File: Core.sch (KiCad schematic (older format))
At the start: 2 parts

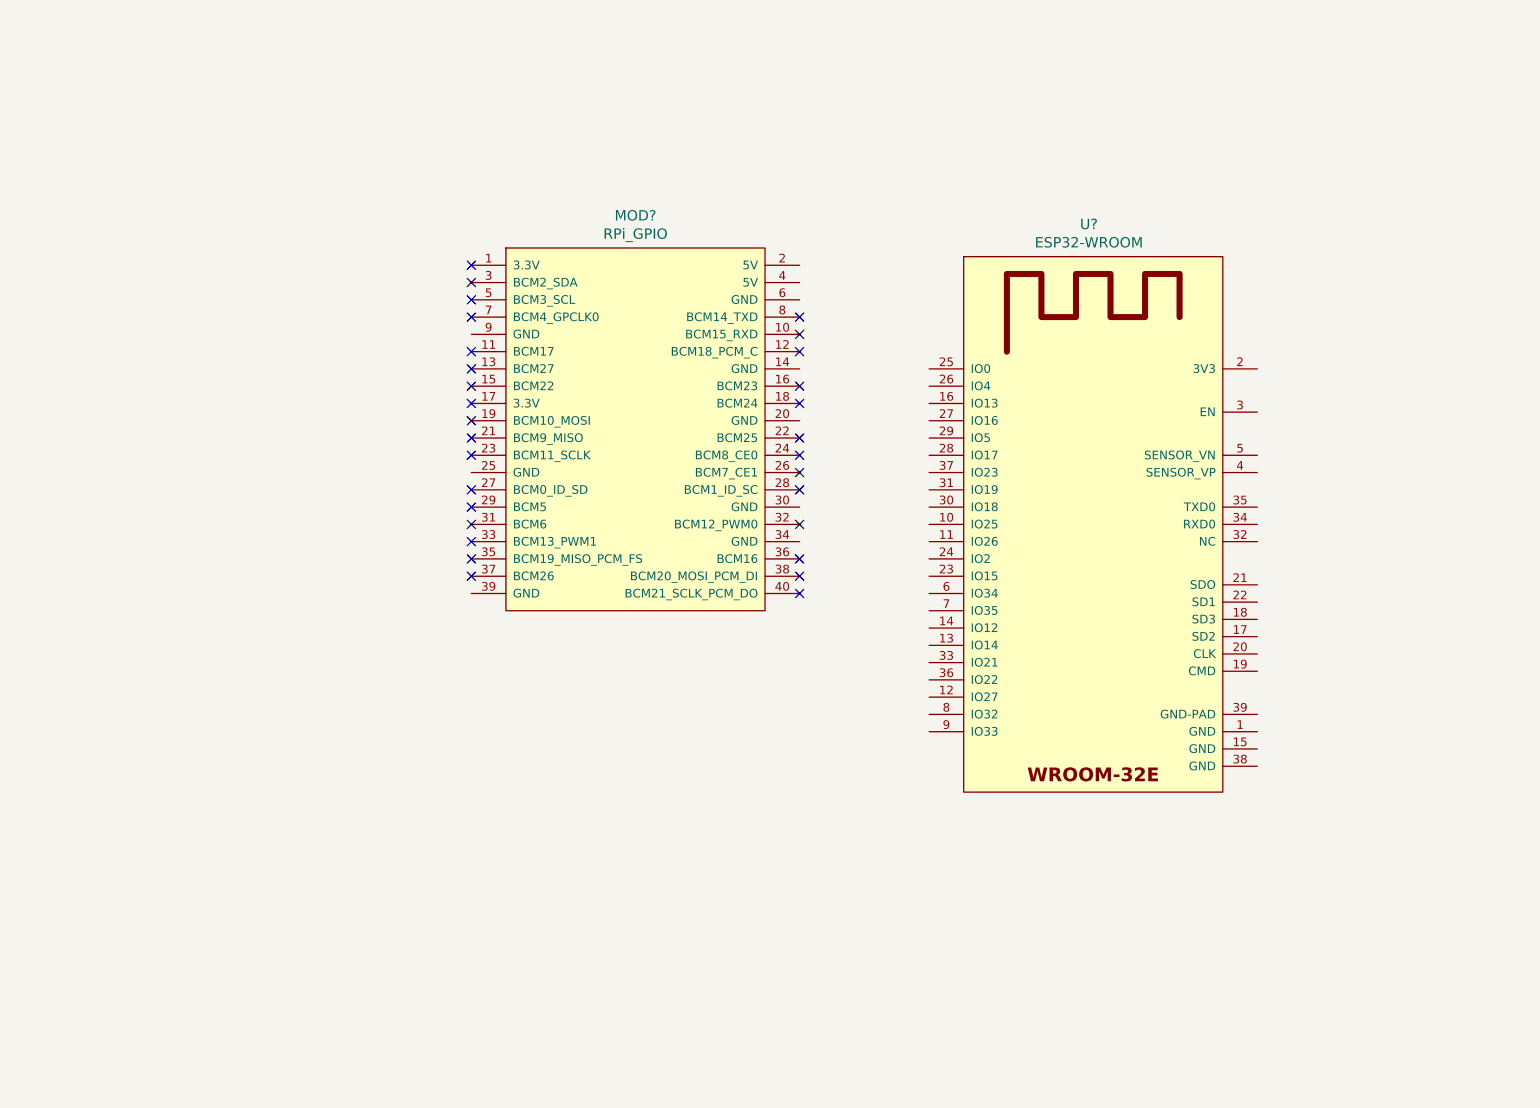
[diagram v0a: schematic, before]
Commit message: Arreglos.
    * Arreglo referencias de address de salida(PCF8574)
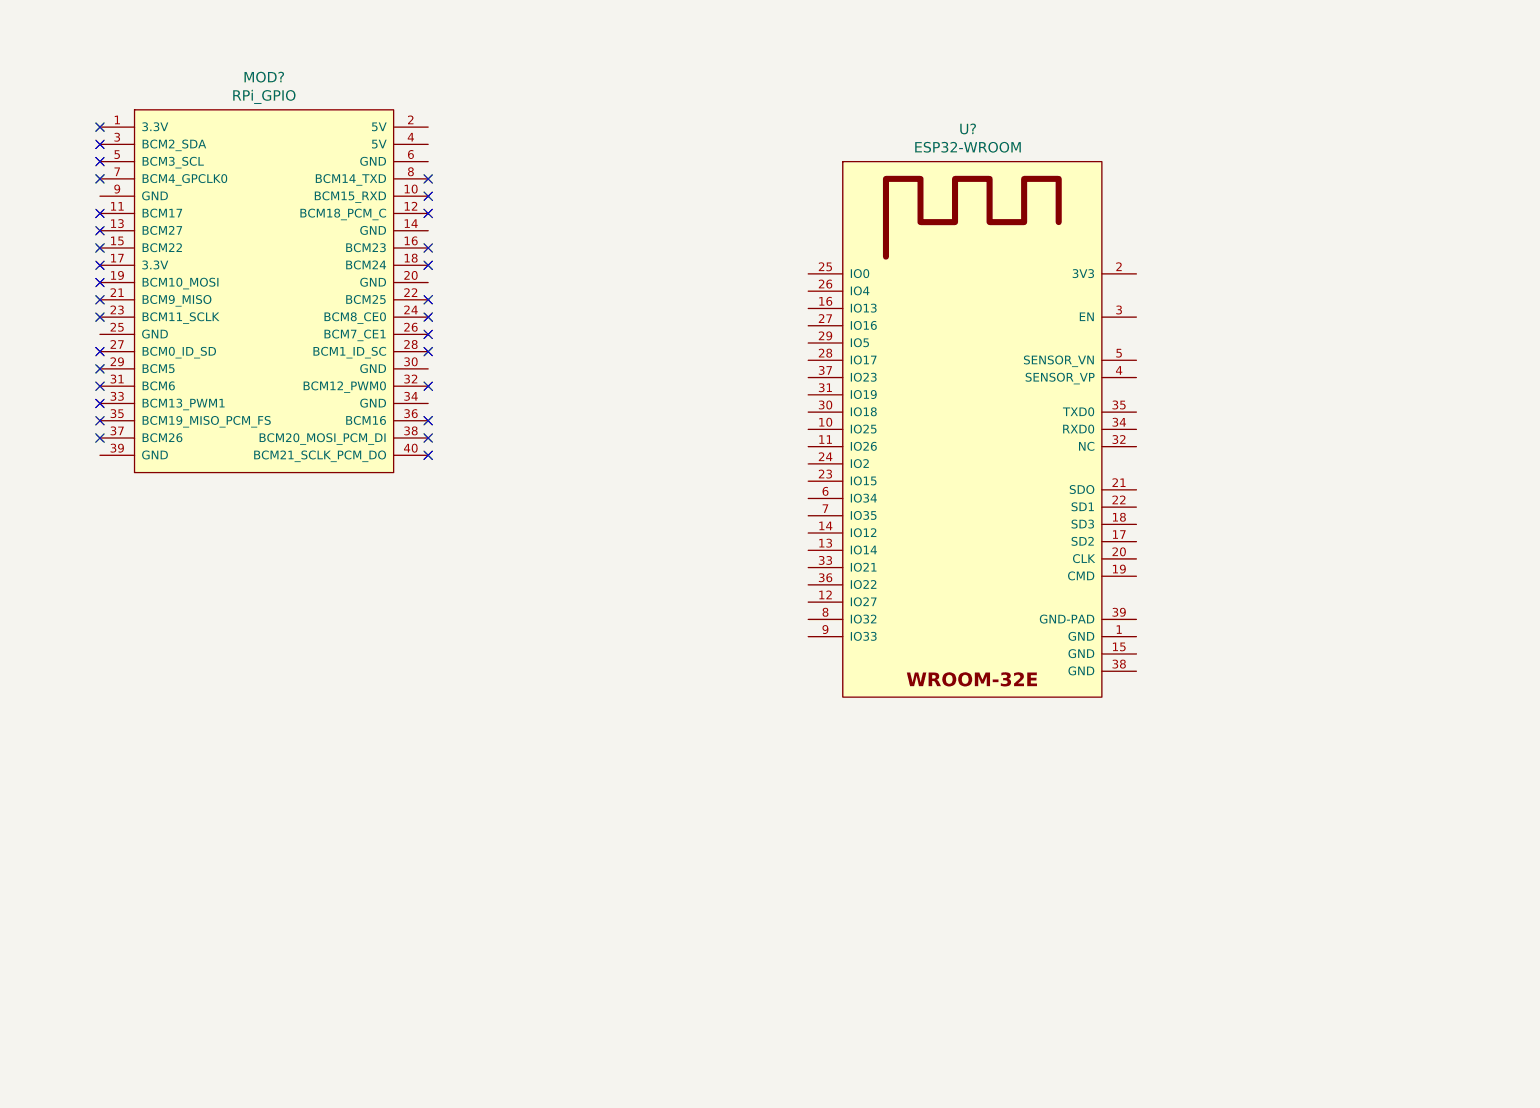
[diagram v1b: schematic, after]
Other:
- moved on the sheet: MOD?, U?
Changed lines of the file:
@@
 L 00_lib_sch:RPi_GPIO MOD?
 U 1 1 61414880
-P 3400 2000
+P 1250 1200
 AR Path="/61414880" Ref="MOD?"  Part="1"
 AR Path="/61410FC3/61414880" Ref="MOD?"  Part="1"
-F 0 "MOD?" H 4150 2287 60  0000 C CNN
-F 1 "RPi_GPIO" H 4150 2181 60  0000 C CNN
-F 2 "00_lib_fp:RPi_fp" H 3400 2000 60  0001 C CNN
-F 3 "" H 3400 2000 60  0000 C CNN
-	1    3400 2000
+F 0 "MOD?" H 2000 1487 60  0000 C CNN
+F 1 "RPi_GPIO" H 2000 1381 60  0000 C CNN
+F 2 "00_lib_fp:RPi_fp" H 1250 1200 60  0001 C CNN
+F 3 "" H 1250 1200 60  0000 C CNN
+	1    1250 1200
 	1    0    0    -1
 $EndComp
@@
 L 00_lib_sch:ESP32-WROOM U?
 U 1 1 614148B6
-P 6800 3150
+P 6100 2600
 AR Path="/614148B6" Ref="U?"  Part="1"
 AR Path="/61410FC3/614148B6" Ref="U?"  Part="1"
-F 0 "U?" H 6775 4537 60  0000 C CNN
-F 1 "ESP32-WROOM" H 6775 4431 60  0000 C CNN
-F 2 "00_lib_fp:ESP32-WROOM" H 7150 4500 60  0001 C CNN
-F 3 "" H 6350 3600 60  0001 C CNN
-	1    6800 3150
+F 0 "U?" H 6075 3987 60  0000 C CNN
+F 1 "ESP32-WROOM" H 6075 3881 60  0000 C CNN
+F 2 "00_lib_fp:ESP32-WROOM" H 6450 3950 60  0001 C CNN
+F 3 "" H 5650 3050 60  0001 C CNN
+	1    6100 2600
 	1    0    0    -1
 $EndComp
-NoConn ~ 3200 2100
-NoConn ~ 3200 2200
-NoConn ~ 3200 2300
-NoConn ~ 3200 2500
-NoConn ~ 3200 2600
-NoConn ~ 3200 2700
-NoConn ~ 3200 2800
-NoConn ~ 3200 2000
-NoConn ~ 3200 2900
-NoConn ~ 3200 3000
-NoConn ~ 3200 3100
-NoConn ~ 3200 3300
-NoConn ~ 3200 3400
-NoConn ~ 3200 3500
-NoConn ~ 3200 3600
-NoConn ~ 3200 3700
-NoConn ~ 3200 3800
-NoConn ~ 5100 3900
-NoConn ~ 5100 3800
-NoConn ~ 5100 3700
-NoConn ~ 5100 3500
-NoConn ~ 5100 3300
-NoConn ~ 5100 3200
-NoConn ~ 5100 3100
-NoConn ~ 5100 3000
-NoConn ~ 5100 2800
-NoConn ~ 5100 2700
-NoConn ~ 5100 2500
-NoConn ~ 5100 2400
-NoConn ~ 5100 2300
+NoConn ~ 1050 1300
+NoConn ~ 1050 1400
+NoConn ~ 1050 1500
+NoConn ~ 1050 1700
+NoConn ~ 1050 1800
+NoConn ~ 1050 1900
+NoConn ~ 1050 2000
+NoConn ~ 1050 1200
+NoConn ~ 1050 2100
+NoConn ~ 1050 2200
+NoConn ~ 1050 2300
+NoConn ~ 1050 2500
+NoConn ~ 1050 2600
+NoConn ~ 1050 2700
+NoConn ~ 1050 2800
+NoConn ~ 1050 2900
+NoConn ~ 1050 3000
+NoConn ~ 2950 3100
+NoConn ~ 2950 3000
+NoConn ~ 2950 2900
+NoConn ~ 2950 2700
+NoConn ~ 2950 2500
+NoConn ~ 2950 2400
+NoConn ~ 2950 2300
+NoConn ~ 2950 2200
+NoConn ~ 2950 2000
+NoConn ~ 2950 1900
+NoConn ~ 2950 1700
+NoConn ~ 2950 1600
+NoConn ~ 2950 1500
 $EndSCHEMATC

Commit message: Agrego v1.0 de SmartSaffron
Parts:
- added C301, C302, C303, C305: 100n, 00_lib_fp:C_0805_2012Metric_Pad1.18x1.45mm_HandSolder, symbol 00_lib_sch:C
- added C304: 10u, 00_lib_fp:C_0805_2012Metric_Pad1.18x1.45mm_HandSolder, symbol 00_lib_sch:CP1
- added D301, D302: WS2812, 00_lib_fp:LED_WS2812_PLCC6_5.0x5.0mm_P1.6mm, symbol 00_lib_sch:WS2812
- added J301: BOOT_Mode, 00_lib_fp:PinHeader_1x02_P2.54mm_Vertical, symbol 00_lib_sch:Conn_01x02
- added J302: Debug_PROG, 00_lib_fp:PinHeader_1x03_P2.54mm_Vertical, symbol Connector_Generic:Conn_01x03
- added R301: 10k, 00_lib_fp:R_0805_2012Metric_Pad1.20x1.40mm_HandSolder, symbol 00_lib_sch:R
- MOD301: renamed from MOD?; footprint 00_lib_fp:RPi_fp -> 00_lib_fp:PinSocket_2x20_P2.54mm_Vertical_SMD
- gave numbers to parts that had none: 1
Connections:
- net GND: now reaches MOD301.14 (GND)
- net GND: now also MOD301.20 (GND), MOD301.30 (GND), MOD301.34 (GND), MOD301.39 (GND), MOD301.6 (GND), MOD301.9 (GND), U301.1 (GND), U301.15 (GND), U301.38 (GND), U301.39 (GND-PAD), C301.2, C302.2, C303.2, C304.2, C305.2, D301.6 (VSS), D302.6 (VSS), J301.2 (Pin_2), J302.3 (Pin_3)
- net +5V: now reaches MOD301.2 (5V)
- net +5V: now also MOD301.4 (5V), C302.1, C303.1, D301.3 (VCC), D301.5 (VDD), D302.3 (VCC), D302.5 (VDD)
- net [YELLOW_ALERT_uC]: now reaches U301.10 (IO25)
- net [SCL1_uC]: now reaches U301.11 (IO26)
- net [SCL2_uC]: now reaches U301.13 (IO14)
- net [SDA2_uC]: now reaches U301.14 (IO12)
- net [ADC_uC]: now reaches U301.16 (IO13)
- net +3V3: now reaches U301.2 (3V3)
- net +3V3: now also C304.1, C305.1, R301.1
- net [SDA1_uC]: now reaches U301.24 (IO2)
- net uC_BOOT: now reaches U301.25 (IO0)
- net uC_BOOT: now also J301.1 (Pin_1)
- net [SDA3_uC]: now reaches U301.26 (IO4)
- net [GREEN_ALERT_uC]: now reaches U301.27 (IO16)
- net LED_LIVE: now reaches U301.28 (IO17)
- net LED_LIVE: now also D301.2 (DIN)
- net at U301.3 (EN): now also C301.1, R301.2
- net [RED_ALERT_uC]: now reaches U301.30 (IO18)
- net [SCL3_uC]: now reaches U301.31 (IO19)
- net uC_RX0: now reaches U301.34 (RXD0)
- net uC_RX0: now also J302.2 (Pin_2)
- net uC_TX0: now reaches U301.35 (TXD0)
- net uC_TX0: now also J302.1 (Pin_1)
- net [SOUND_ALERT_uC]: now reaches U301.7 (IO35)
- net [TX_uC]: now reaches U301.8 (IO32)
- net [RX_uC]: now reaches U301.9 (IO33)
- new net: D301.1 (DOUT), D302.2 (DIN)
- no-connect marks 30 -> 47
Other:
- note added: "CORE"
- note added: "Capacitores de desacople.\nColocar lo mas cercano posible \na los pines del IC en cuestion."
- moved on the sheet: MOD301, U301

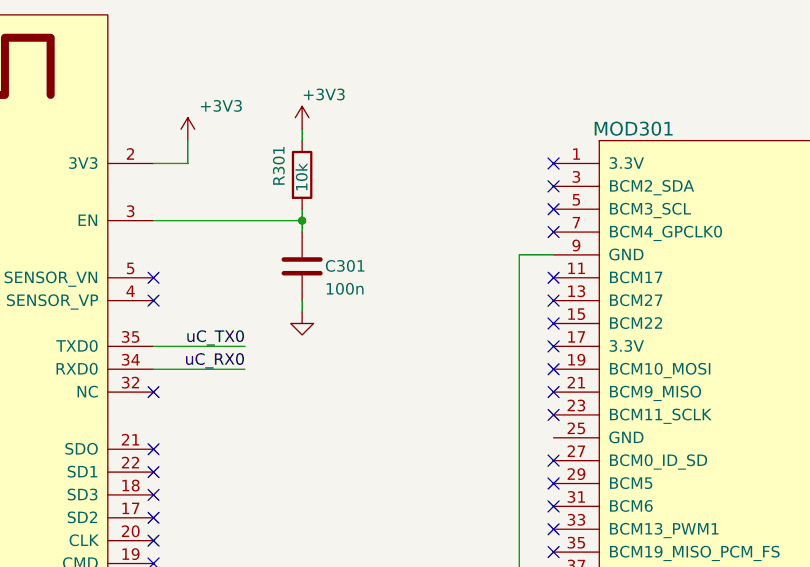
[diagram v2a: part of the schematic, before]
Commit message: Fixes PCB, reset esp32
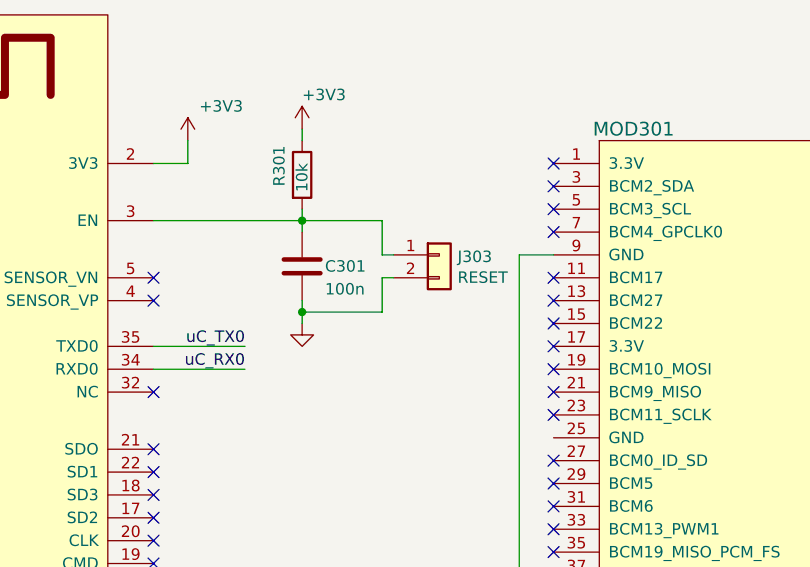
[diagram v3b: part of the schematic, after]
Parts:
- added J303: RESET, 00_lib_fp:PinHeader_1x02_P2.54mm_Vertical, symbol 00_lib_sch:Conn_01x02
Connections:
- net GND: now also J303.2 (Pin_2)
- net at C301.1, R301.2, U301.3 (EN): now also J303.1 (Pin_1)
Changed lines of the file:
@@
 L 00_lib_sch:GND #PWR0227
 U 1 1 614AEF2F
-P 6050 3050
-F 0 "#PWR0227" H 6050 2800 50  0001 C CNN
-F 1 "GND" H 6055 2877 50  0001 C CNN
-F 2 "" H 6050 3050 50  0001 C CNN
-F 3 "" H 6050 3050 50  0001 C CNN
-	1    6050 3050
+P 6050 3100
+F 0 "#PWR0227" H 6050 2850 50  0001 C CNN
+F 1 "GND" H 6055 2927 50  0001 C CNN
+F 2 "" H 6050 3100 50  0001 C CNN
+F 3 "" H 6050 3100 50  0001 C CNN
+	1    6050 3100
 	1    0    0    -1
 $EndComp
@@
 	6050 2250 6050 2300
 Wire Wire Line
-	6050 3050 6050 3000
+	6050 3100 6050 3050
 Wire Wire Line
 	5400 2400 5550 2400
@@
 NoConn ~ 3500 4200
 NoConn ~ 3500 4300
+$Comp
+L 00_lib_sch:Conn_01x02 J303
+U 1 1 6172D5A8
+P 6650 2800
+F 0 "J303" H 6730 2792 50  0000 L CNN
+F 1 "RESET" H 6730 2701 50  0000 L CNN
+F 2 "00_lib_fp:PinHeader_1x02_P2.54mm_Vertical" H 6650 2800 50  0001 C CNN
+F 3 "" H 6650 2800 50  0001 C CNN
+	1    6650 2800
+	1    0    0    -1
+$EndComp
+Wire Wire Line
+	6400 2800 6400 2650
+Wire Wire Line
+	6400 2650 6050 2650
+Wire Wire Line
+	6400 2800 6450 2800
+Wire Wire Line
+	6400 3050 6400 2900
+Wire Wire Line
+	6400 2900 6450 2900
+Wire Wire Line
+	6050 3050 6400 3050
+Connection ~ 6050 3050
+Wire Wire Line
+	6050 3050 6050 3000
 $EndSCHEMATC

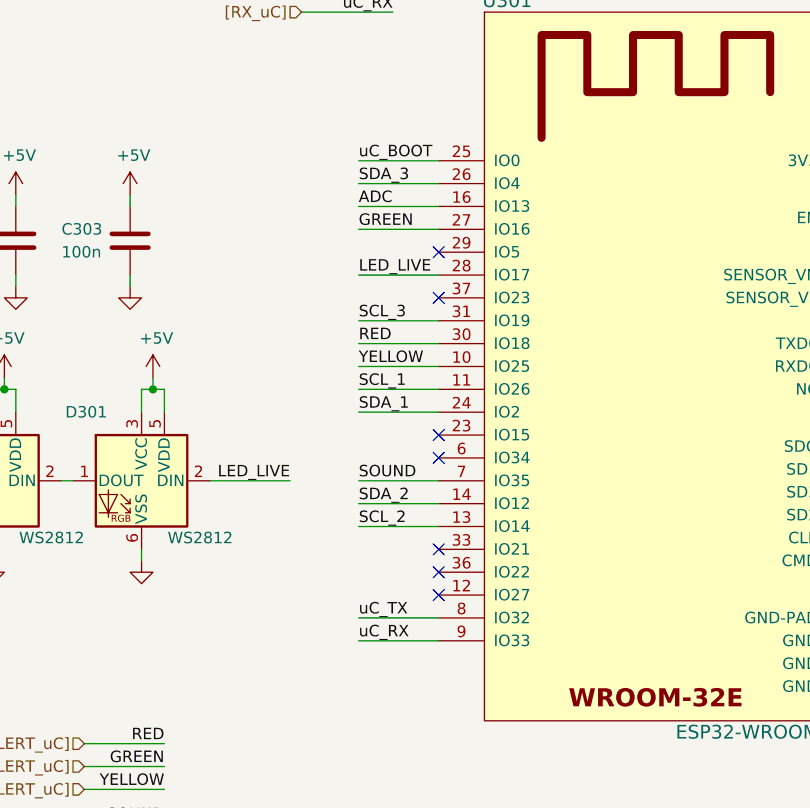
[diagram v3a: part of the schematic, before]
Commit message: Fix por revision grupal
    *Fix de memoria de i2c, mal sda y scl
    *Fix inpunts sda y scl
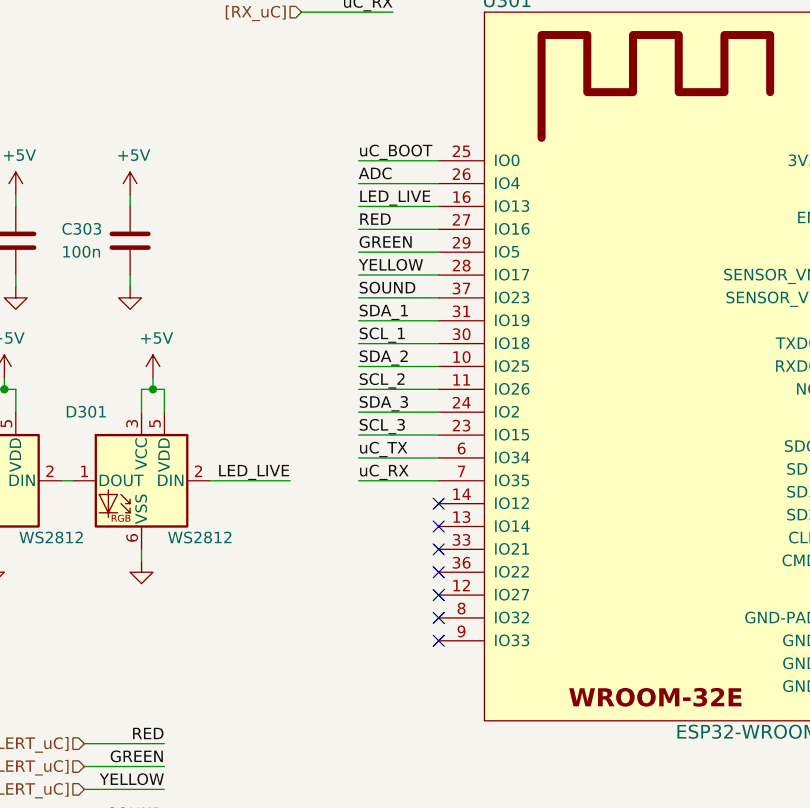
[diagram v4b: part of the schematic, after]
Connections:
- net LED_LIVE: now also U301.16 (IO13); no longer U301.28 (IO17)
- net [ADC_uC]: now also U301.26 (IO4); no longer U301.16 (IO13)
- net [GREEN_ALERT_uC]: now also U301.29 (IO5); no longer U301.27 (IO16)
- net [RED_ALERT_uC]: now also U301.27 (IO16); no longer U301.30 (IO18)
- net [RX_uC]: now also U301.7 (IO35); no longer U301.9 (IO33)
- net [SCL1_uC]: now also U301.30 (IO18); no longer U301.11 (IO26)
- net [SCL2_uC]: now also U301.11 (IO26); no longer U301.13 (IO14)
- net [SCL3_uC]: now also U301.23 (IO15); no longer U301.31 (IO19)
- net [SDA1_uC]: now also U301.31 (IO19); no longer U301.24 (IO2)
- net [SDA2_uC]: now also U301.10 (IO25); no longer U301.14 (IO12)
- net [SDA3_uC]: now also U301.24 (IO2); no longer U301.26 (IO4)
- net [SOUND_ALERT_uC]: now also U301.37 (IO23); no longer U301.7 (IO35)
- net [TX_uC]: now also U301.6 (IO34); no longer U301.8 (IO32)
- net [YELLOW_ALERT_uC]: now also U301.28 (IO17); no longer U301.10 (IO25)
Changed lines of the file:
@@
-	1    0    0    -1
-$EndComp
-$Comp
-L 00_lib_sch:ESP32-WROOM U?
-U 1 1 614148B6
-P 4450 2950
-AR Path="/614148B6" Ref="U?"  Part="1"
-AR Path="/61410FC3/614148B6" Ref="U301"  Part="1"
-F 0 "U301" H 3800 4200 60  0000 C CNN
-F 1 "ESP32-WROOM" H 4850 1000 60  0000 C CNN
-F 2 "00_lib_fp:ESP32-WROOM" H 4800 4300 60  0001 C CNN
-F 3 "" H 4000 3400 60  0001 C CNN
-	1    4450 2950
 	1    0    0    -1
 $EndComp
@@
 SOUND
 Wire Wire Line
-	3500 3800 3150 3800
-Text Label 3150 3800 0    50   ~ 0
+	3500 3000 3150 3000
+Text Label 3150 3000 0    50   ~ 0
 SOUND
 Wire Wire Line
@@
 SCL_1
 Wire Wire Line
-	3500 3500 3150 3500
-Text Label 3150 3500 0    50   ~ 0
+	3500 3100 3150 3100
+Text Label 3150 3100 0    50   ~ 0
 SDA_1
 Wire Wire Line
-	3500 3400 3150 3400
-Text Label 3150 3400 0    50   ~ 0
+	3500 3200 3150 3200
+Text Label 3150 3200 0    50   ~ 0
 SCL_1
 Wire Wire Line
@@
 YELLOW
 Wire Wire Line
-	3500 3200 3150 3200
-Text Label 3150 3200 0    50   ~ 0
-RED
-Wire Wire Line
 	3500 2700 3150 2700
 Text Label 3150 2700 0    50   ~ 0
+RED
+Wire Wire Line
+	3500 2800 3150 2800
+Text Label 3150 2800 0    50   ~ 0
 GREEN
 Wire Wire Line
-	3500 3300 3150 3300
-Text Label 3150 3300 0    50   ~ 0
+	3500 2900 3150 2900
+Text Label 3150 2900 0    50   ~ 0
 YELLOW
 Wire Wire Line
-	3500 2500 3150 2500
-Text Label 3150 2500 0    50   ~ 0
+	3500 3500 3150 3500
+Text Label 3150 3500 0    50   ~ 0
 SDA_3
 Wire Wire Line
-	3500 3100 3150 3100
-Text Label 3150 3100 0    50   ~ 0
+	3500 3600 3150 3600
+Text Label 3150 3600 0    50   ~ 0
 SCL_3
 Wire Wire Line
@@
 SCL_3
 Wire Wire Line
-	3500 2900 3150 2900
-Text Label 3150 2900 0    50   ~ 0
+	3500 2600 3150 2600
+Text Label 3150 2600 0    50   ~ 0
 LED_LIVE
 Wire Wire Line
@@
 LED_LIVE
 Wire Wire Line
-	3500 4500 3150 4500
-Wire Wire Line
-	3500 4400 3150 4400
-Text Label 3150 4400 0    50   ~ 0
+	3500 3800 3150 3800
+Wire Wire Line
+	3500 3700 3150 3700
+Text Label 3150 3700 0    50   ~ 0
 uC_TX
-Text Label 3150 4500 0    50   ~ 0
+Text Label 3150 3800 0    50   ~ 0
 uC_RX
 Wire Wire Line
-	3500 4000 3150 4000
-Text Label 3150 3900 0    50   ~ 0
+	3500 3400 3150 3400
+Text Label 3150 3300 0    50   ~ 0
 SDA_2
 Wire Wire Line
-	3500 3900 3150 3900
-Text Label 3150 4000 0    50   ~ 0
+	3500 3300 3150 3300
+Text Label 3150 3400 0    50   ~ 0
 SCL_2
 Wire Wire Line
@@
 Text Label 2300 6250 2    50   ~ 0
 ADC
-Text Label 3150 2600 0    50   ~ 0
+Text Label 3150 2500 0    50   ~ 0
 ADC
 Wire Wire Line
-	3150 2600 3500 2600
-NoConn ~ 3500 2800
-NoConn ~ 3500 3000
-NoConn ~ 3500 3600
-NoConn ~ 3500 3700
+	3150 2500 3500 2500
 NoConn ~ 3500 4100
 NoConn ~ 3500 4200
@@
 Wire Wire Line
 	6050 3050 6050 3000
+$Comp
+L 00_lib_sch:ESP32-WROOM U?
+U 1 1 614148B6
+P 4450 2950
+AR Path="/614148B6" Ref="U?"  Part="1"
+AR Path="/61410FC3/614148B6" Ref="U301"  Part="1"
+F 0 "U301" H 3800 4200 60  0000 C CNN
+F 1 "ESP32-WROOM" H 4850 1000 60  0000 C CNN
+F 2 "00_lib_fp:ESP32-WROOM" H 4800 4300 60  0001 C CNN
+F 3 "" H 4000 3400 60  0001 C CNN
+	1    4450 2950
+	1    0    0    -1
+$EndComp
+NoConn ~ 3500 3900
+NoConn ~ 3500 4000
+NoConn ~ 3500 4400
+NoConn ~ 3500 4500
 $EndSCHEMATC
